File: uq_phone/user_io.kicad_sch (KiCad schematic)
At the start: 17 parts, among them J5 KP15B-6S-SF_800_, J7 Conn_01x02, J8 541324562, U12 MCP1664T-E/OT, U14 TPD8F003DQDR, U8 LSM6DSVTR, U9 DRV2603RUNR

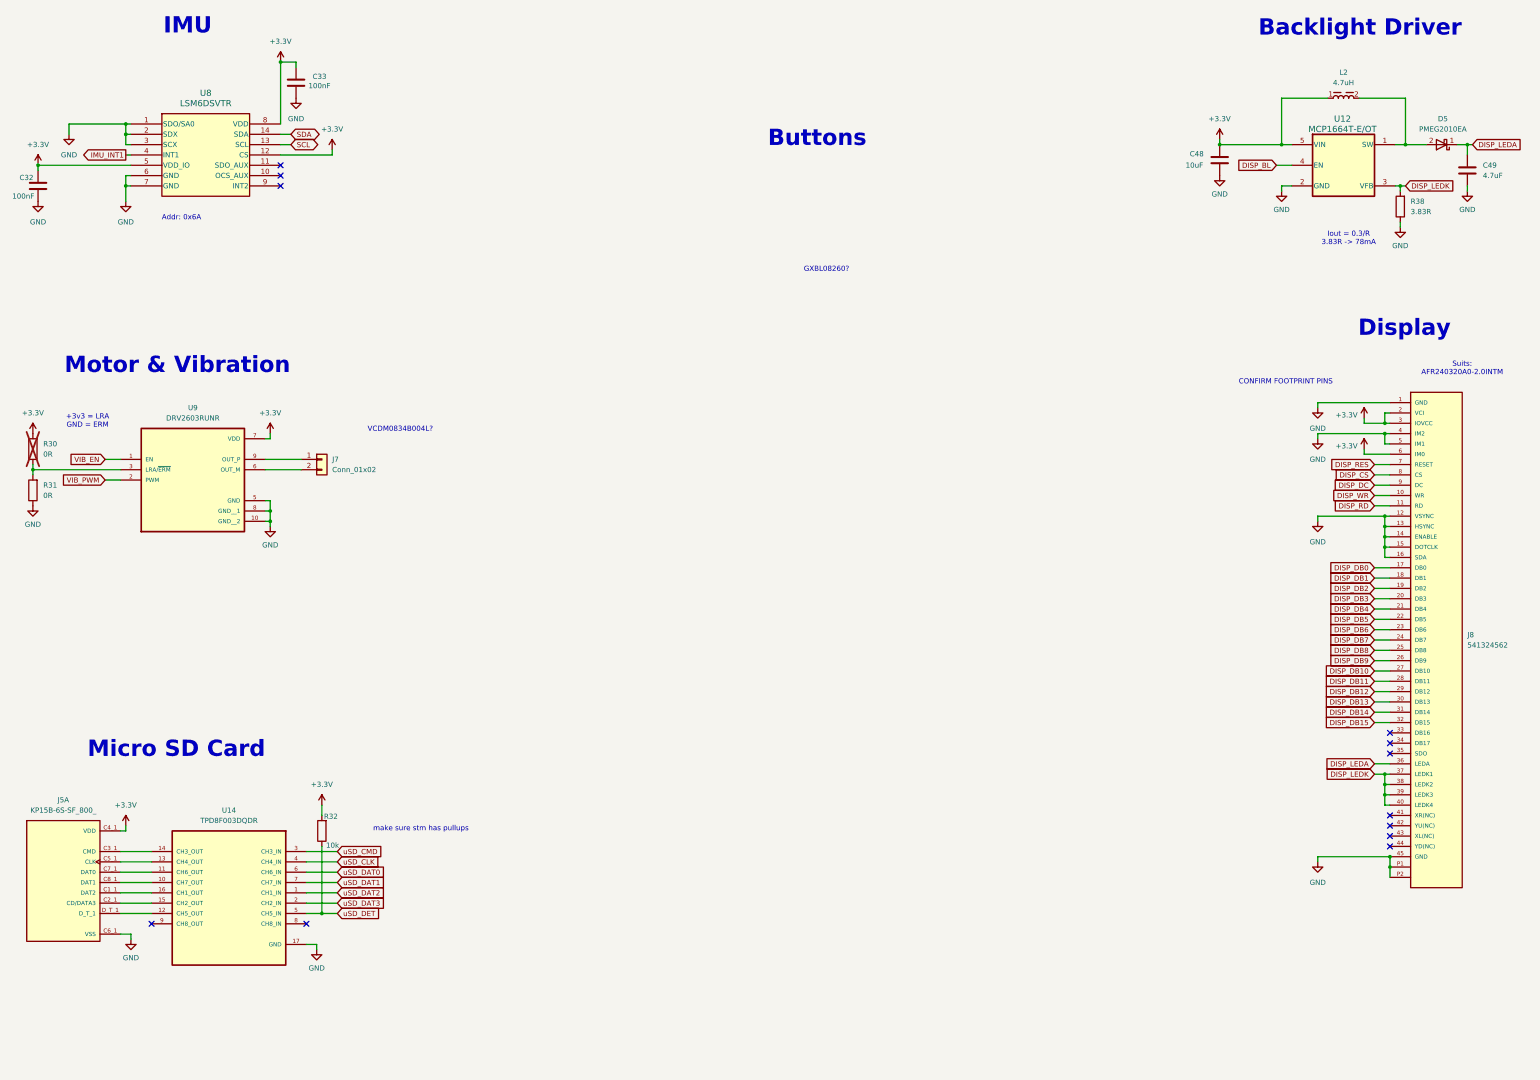
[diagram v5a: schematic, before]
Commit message: Add LEDs, Inital Buttons
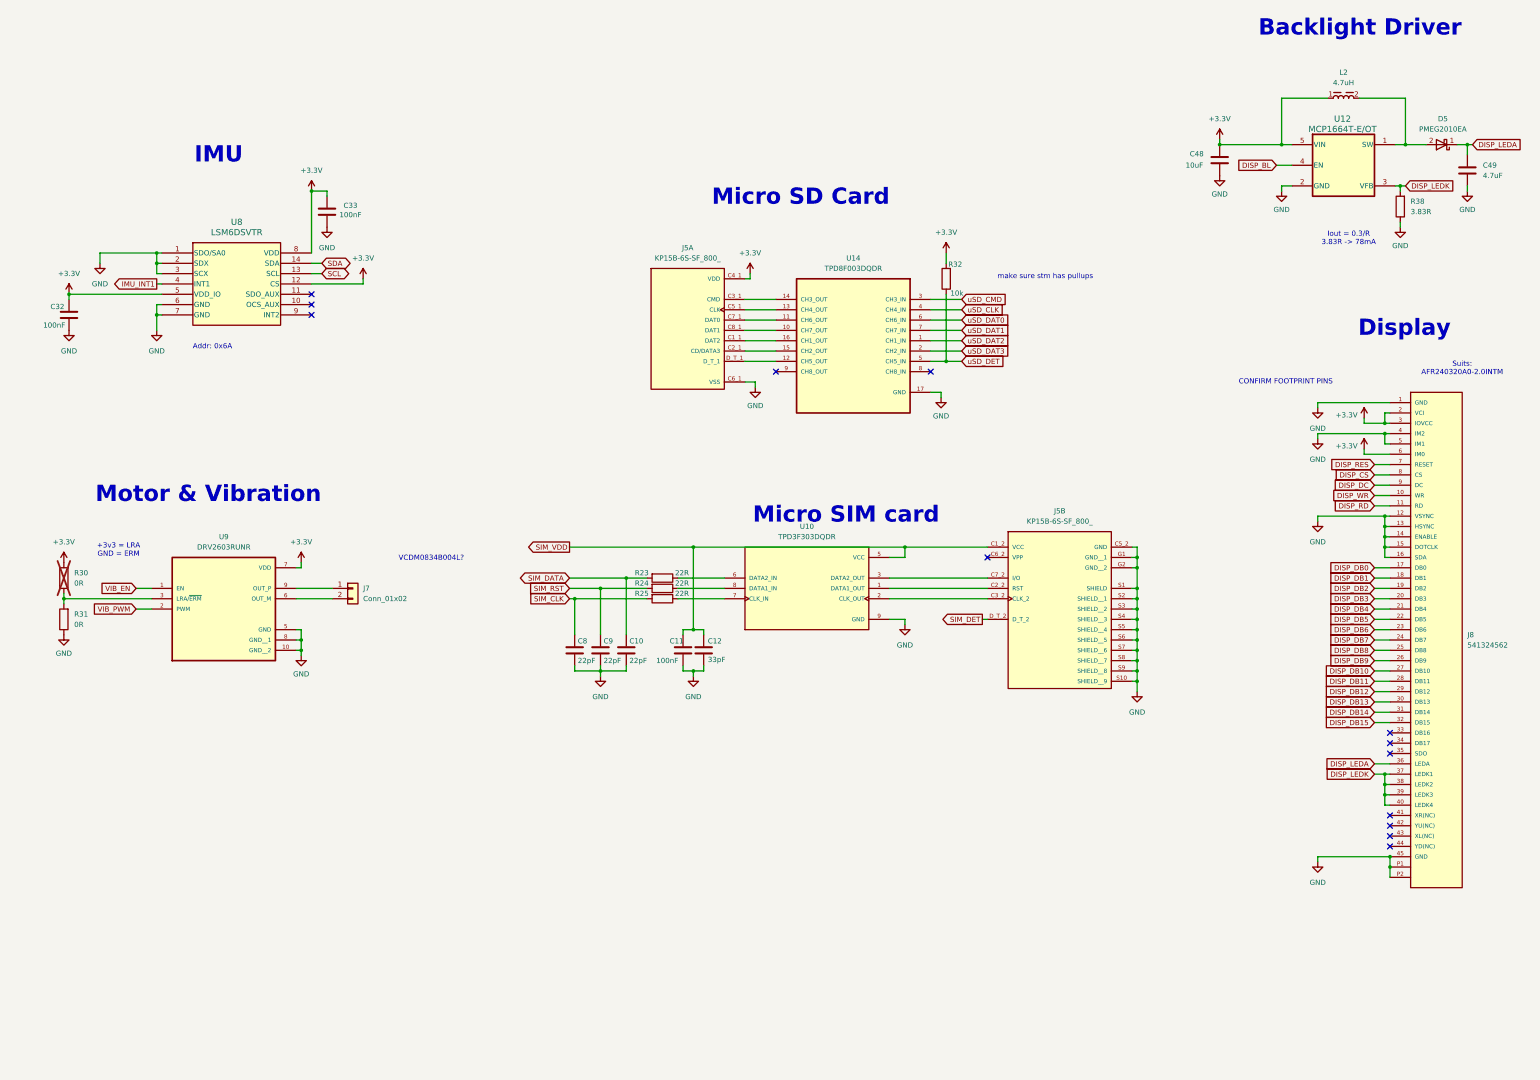
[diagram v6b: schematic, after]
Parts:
- added C10, C8, C9: 22pF, Capacitor_SMD:C_0402_1005Metric, symbol Capacitors:Capacitor_22pF
- added C11: 100nF, Capacitor_SMD:C_0402_1005Metric, symbol Capacitors:capacitor_100nF
- added C12: 33pF, Capacitor_SMD:C_0402_1005Metric, symbol Capacitors:Capacitor_33pF
- added unit 2 of J5
- added R23, R24, R25: 22R, Resistor_SMD:R_0402_1005Metric, symbol Resistors:Resistor_22R
- added U10: TPD3F303DQDR, TPD3F303DQDR:SON40P170X135X80-9N, symbol TPD3F303DQDR:TPD3F303DQDR
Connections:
- net GND: now also C10.2, C11.2, C12.2, C8.2, C9.2, J5.C5_2 (GND), J5.G1 (GND__1), J5.G2 (GND__2), J5.S1 (SHIELD), J5.S10 (SHIELD__9), J5.S2 (SHIELD__1), J5.S3 (SHIELD__2), J5.S4 (SHIELD__3), J5.S5 (SHIELD__4), J5.S6 (SHIELD__5), J5.S7 (SHIELD__6), J5.S8 (SHIELD__7), J5.S9 (SHIELD__8), U10.9 (GND)
- new net: R23.1, U10.6 (DATA2_IN)
- new net: J5.C2_2 (RST), U10.1 (DATA1_OUT)
- new net: J5.C3_2 (CLK_2), U10.2 (CLK_OUT)
- new net: J5.C7_2 (I/O), U10.3 (DATA2_OUT)
- new net: R25.1, U10.7 (CLK_IN)
- new net: R24.1, U10.8 (DATA1_IN)
- new net SIM_CLK: C8.1, R25.2
- new net SIM_DATA: C10.1, R23.2
- new net SIM_DET: J5.D_T_2
- new net SIM_RST: C9.1, R24.2
- new net SIM_VDD: C11.1, C12.1, J5.C1_2 (VCC), U10.5 (VCC)
- no-connect marks 12 -> 13
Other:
- note added: "Micro SIM card"
- note removed: "Buttons"
- note removed: "GXBL08260?"
- moved on the sheet: C32, C33, J5A, J7, R30, R31, R32, U14, U8, U9

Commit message: Routing Init
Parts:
- renumbered C32 to C27, C33 to C28, C8 to C29, C9 to C30, C10 to C31, C11 to C32, C12 to C33, C48 to C34, C49 to C35, D5 to D2, J5 to J8, J8 to J9, R30 to R28, R31 to R29, R23 to R30, R24 to R31, R25 to R32, R32 to R33, R38 to R34, U14 to U11

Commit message: Update routing
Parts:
- added M1: VCDM0834B004L, custom_footprints:Motor_8mm, symbol Misc:VCDM0834B004L
- J7: footprint Connector_Wire:SolderWire-0.15sqmm_1x02_P4mm_D0.5mm_OD1.5mm -> Connector_Wire:SolderWire-0.1sqmm_1x02_P3.6mm_D0.4mm_OD1mm
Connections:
- net IMU_INT1: no longer names the net of U8.4 (INT1)
- no-connect marks 13 -> 14
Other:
- note removed: "VCDM0834B004L?"
- moved on the sheet: C27, C28, C29, C30, C31, C32, C33, J7, J8A, J8B, R28, R29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
